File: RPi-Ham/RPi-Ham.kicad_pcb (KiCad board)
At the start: 2 copper layers, 65 x 56.5 mm, 45 parts, among them J1 Conn_02x03_Counter_Clockwise, J10 MountingHole_2.7mm_M2.5_Pad_V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, J11 MountingHole_2.7mm_M2.5_Pad_V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, J12 MountingHole_2.7mm_M2.5_Pad_V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, J13 MountingHole_2.7mm_M2.5_Pad_V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, J2 RJ45, J3 Conn_02x03_Counter_Clockwise, J4 RJ45, J5 RJ45, J6 Conn_02x08_Counter_Clockwise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

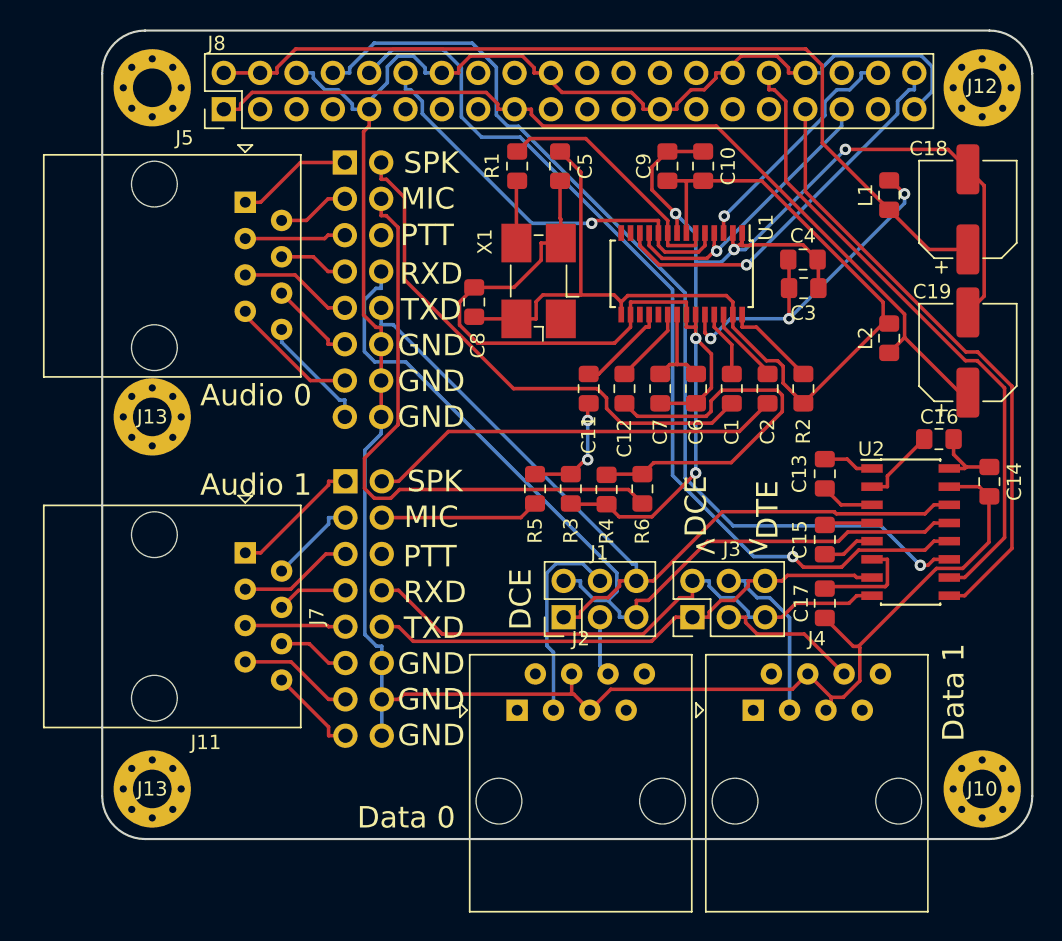
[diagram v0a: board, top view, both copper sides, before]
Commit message: Added PTT
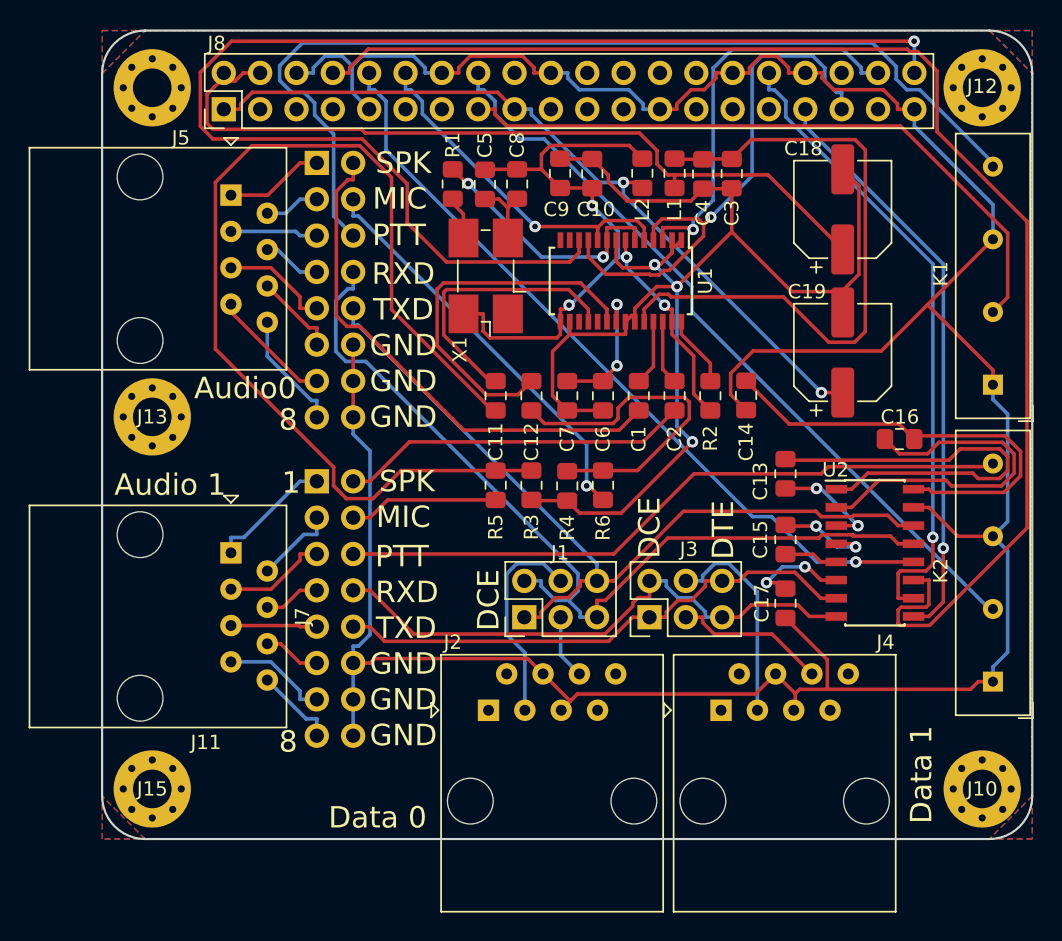
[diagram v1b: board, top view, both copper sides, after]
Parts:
- added K1: SILxx-1Axx-71x, Relay_THT:Relay_SPST_StandexMeder_SIL_Form1A, F.Cu at (109.8, 53.2)
- added K2: SILxx-1Axx-71x, Relay_THT:Relay_SPST_StandexMeder_SIL_Form1A, F.Cu at (109.8, 74.0)
- moved L2 20.7 mm to (85.2, 38.5)
- moved C14 18.0 mm to (92.5, 54.0)
- moved L1 15.1 mm to (87.5, 38.5)
- moved C3 9.45 mm to (91.5, 38.5), turned to 270 degrees
- moved C4 9.18 mm to (89.5, 38.5), turned to 270 degrees
- moved C8 8.78 mm to (76.5, 39.2), turned to 270 degrees
- moved C18 8.75 mm to (99.2, 41.0)
- moved C19 8.75 mm to (99.2, 51.0)
- moved C10 7.77 mm to (81.8, 38.5)
- moved C9 7.52 mm to (79.5, 38.5)
- moved C1 6.52 mm to (85.0, 54.0)
- moved C11 6.52 mm to (75.0, 54.0)
- moved C12 6.52 mm to (77.5, 54.0)
- moved C2 6.52 mm to (87.5, 54.0)
- moved C6 6.52 mm to (82.5, 54.0)
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- renumbered J13 to J15
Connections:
- C5 pad 2: Earth -> Net-(C5-Pad2)
- C8 pad 2: Earth -> Net-(C5-Pad2)
- J8 pad 15: Net-(J8-Pad15) -> PTTL0
- J8 pad 16: Net-(J8-Pad16) -> PTTL1
- X1 pad 2: Earth -> Net-(C5-Pad2)
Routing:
- net PTT0: track 0.00 -> 69.2 mm
- net Net-(C11-Pad2): track 8.07 -> 73.4 mm, vias 2 -> 0
- net DIN: track 27.4 -> 89.9 mm
- net PTTL1: track 0.00 -> 53.7 mm
- net PTT1: track 0.00 -> 47.3 mm
- net PTTL0: track 0.00 -> 46.7 mm
- net GND: track 169.0 -> 213.4 mm
- net Earth: track 128.8 -> 97.4 mm, vias 5 -> 3
- net TXD0: track 69.0 -> 96.2 mm, vias 1 -> 0
- net Net-(C13-Pad1): track 3.57 -> 29.9 mm
- net Net-(C14-Pad2): track 5.16 -> 31.2 mm
- net Net-(C12-Pad1): track 5.40 -> 26.0 mm
- net VDD: track 73.2 -> 53.0 mm, vias 0 -> 4
- net VCC: track 25.6 -> 45.4 mm, vias 3 -> 0
- net Net-(C16-Pad2): track 5.47 -> 25.2 mm
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- added copper zone on B.Cu, net (none)
- added copper zone on F.Cu, net (none)
- added copper zone on B.Cu, net GND
- added copper zone on F.Cu, net GND
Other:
- board text added: "1"
- board text added: "8"
- board text added: "Audio0"
- board text removed: "< >"
- board text removed: "Audio 0"
